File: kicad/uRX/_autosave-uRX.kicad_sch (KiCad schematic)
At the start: 124 parts, among them J1 RF_AM_GND, J2 C165948, J3 AudioJack2_Ground, J4 +5Vfiltered, J5 +5V, J6 U.FL, J7 +3.3Vfiltered, J9 RF_AM__In, Q1 BC847, SW1 RotaryEncoder_Switch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

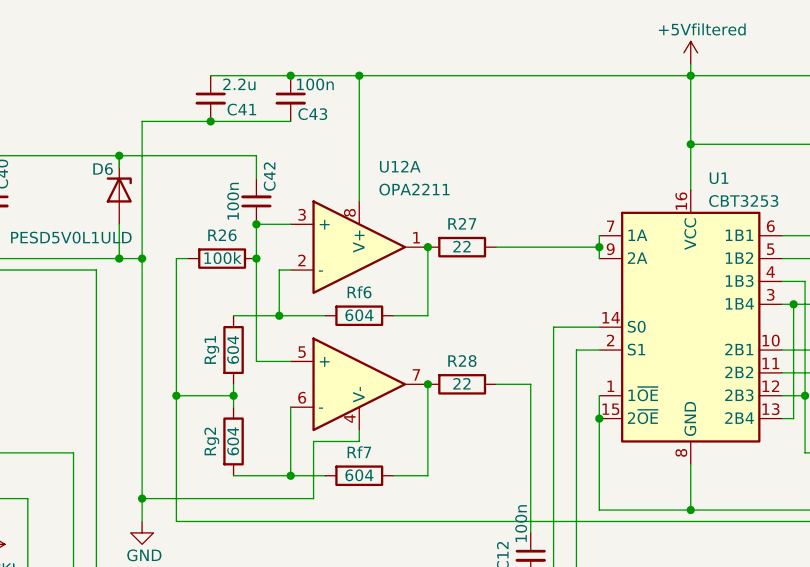
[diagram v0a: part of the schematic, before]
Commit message: work on rf part pcb
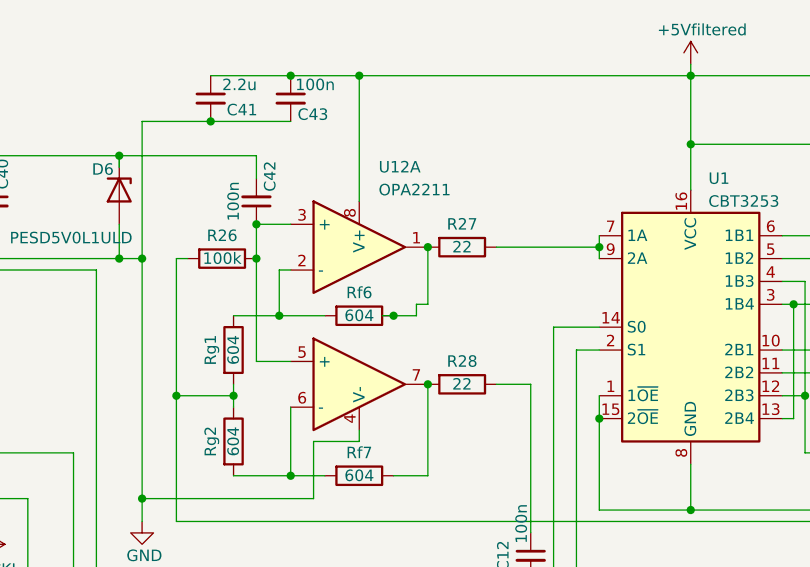
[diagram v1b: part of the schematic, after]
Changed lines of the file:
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@@
 	)
 	(junction
+		(at 165.1 44.45)
+		(diameter 0)
+		(color 0 0 0 0)
+	)
+	(junction
 		(at 86.36 189.23)
 		(diameter 0)
@@
 	(wire
 		(pts
-			(xy 165.1 44.45) (xy 168.91 44.45)
+			(xy 163.83 44.45) (xy 165.1 44.45)
 		)
 		(stroke
@@
 	(wire
 		(pts
+			(xy 165.1 44.45) (xy 167.64 44.45)
+		)
+		(stroke
+			(width 0)
+			(type default)
+		)
+	)
+	(wire
+		(pts
 			(xy 105.41 162.56) (xy 100.33 162.56)
 		)
@@
 	(wire
 		(pts
-			(xy 168.91 44.45) (xy 168.91 36.83)
+			(xy 167.64 44.45) (xy 167.64 43.18)
 		)
 		(stroke
@@
 	(wire
 		(pts
+			(xy 167.64 43.18) (xy 168.91 43.18)
+		)
+		(stroke
+			(width 0)
+			(type default)
+		)
+	)
+	(wire
+		(pts
 			(xy 251.46 146.05) (xy 280.67 146.05)
 		)
@@
 		)
 		(stroke
+			(width 0)
+			(type default)
+		)
+	)
+	(wire
+		(pts
+			(xy 168.91 43.18) (xy 168.91 36.83)
+		)
+		(stroke
